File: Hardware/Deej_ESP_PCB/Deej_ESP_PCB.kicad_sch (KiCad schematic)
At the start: 110 parts, among them J1 USB_C_Receptacle_USB2.0_16P, P1 10K, P2 10K, P3 10K, P4 10K, P5 10K, P6 10K, SW1 SW_Push, SW2 SW_Push, SW3 SW_Push, SW4 SW_Push, SW5 SW_Push, SW6 SW_Push, U1 ESP32-S3-MINI-1U, U10 0.96" 128x64 OLED, U11 ECMF02-2AMX6, U2 PCF8574RGTR, U3 PCF8574RGTR, U4 PCF8574RGTR, U5 SN74HCS126DR, U6 SN74HCS126DR, U7 0.96" 128x64 OLED, U8 0.96" 128x64 OLED, U9 0.96" 128x64 OLED

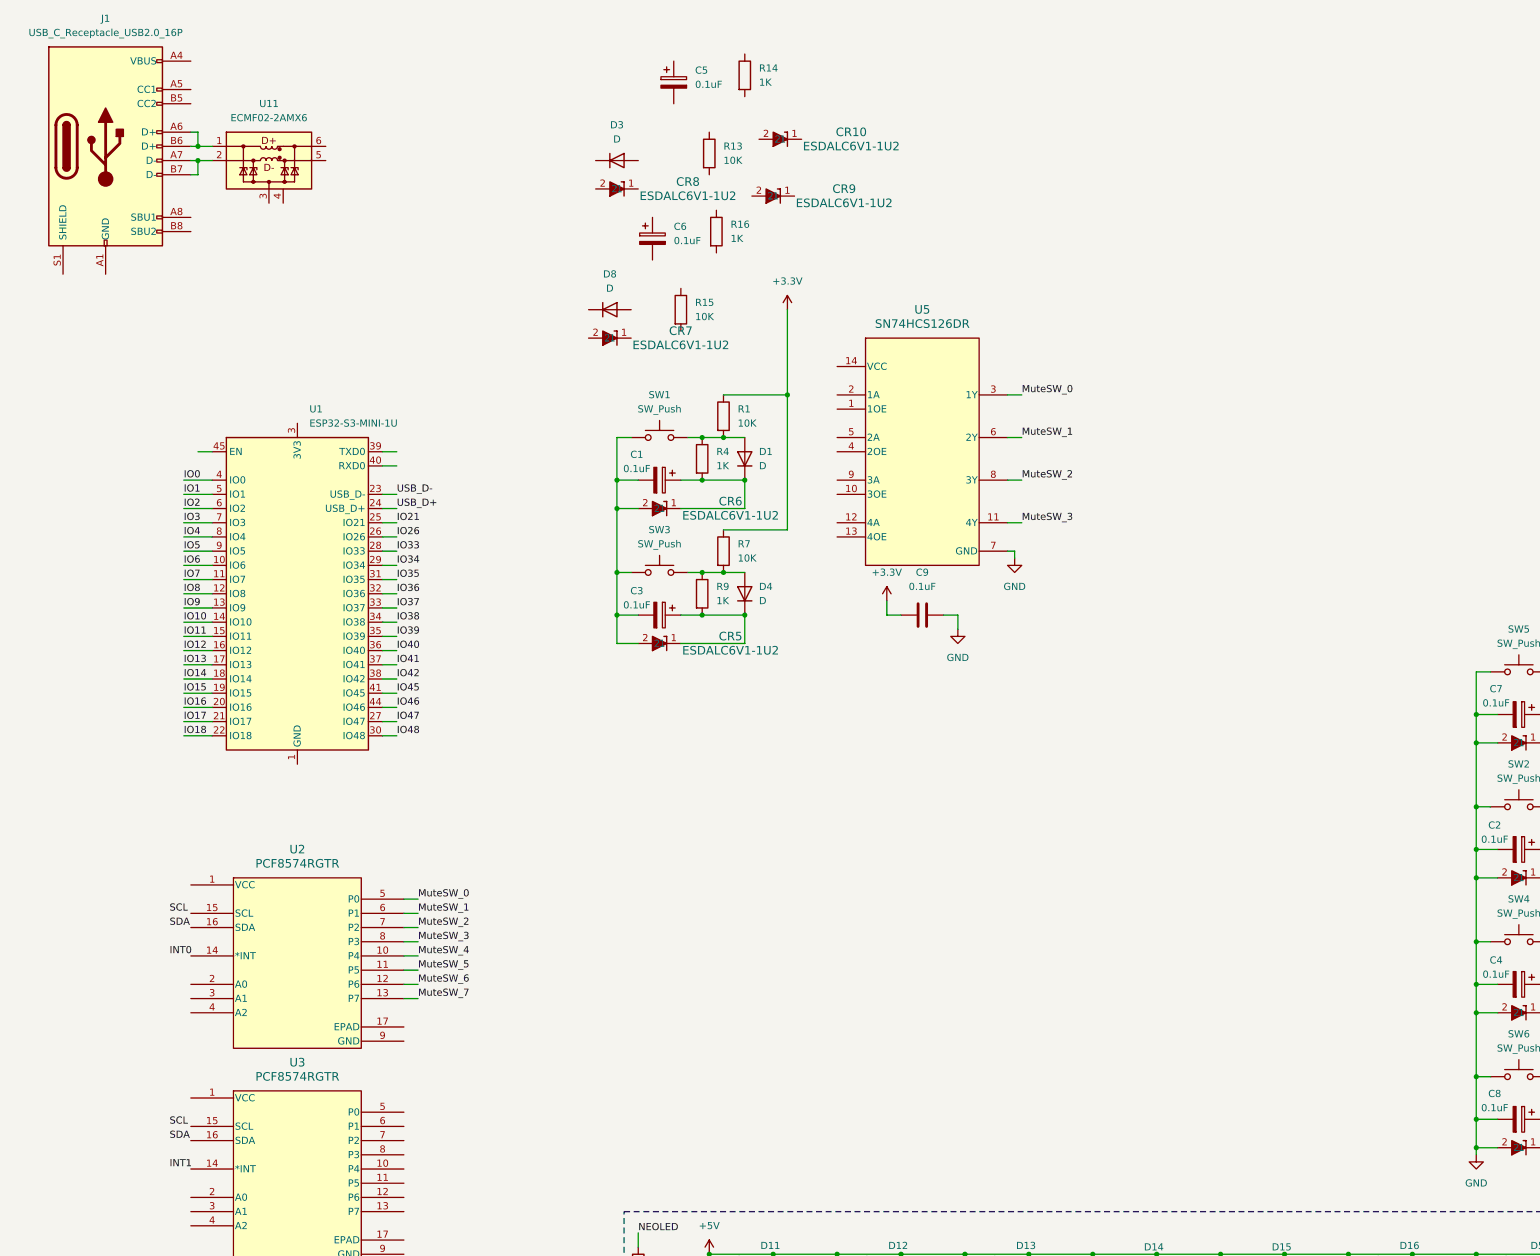
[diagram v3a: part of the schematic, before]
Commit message: USB Supporting Hardware, 3D Models, BOM Updates
* Added supporting hardware for the USB C connector
* Ensured all current components have 3D models
* Updated the BOM with components for the USB connector
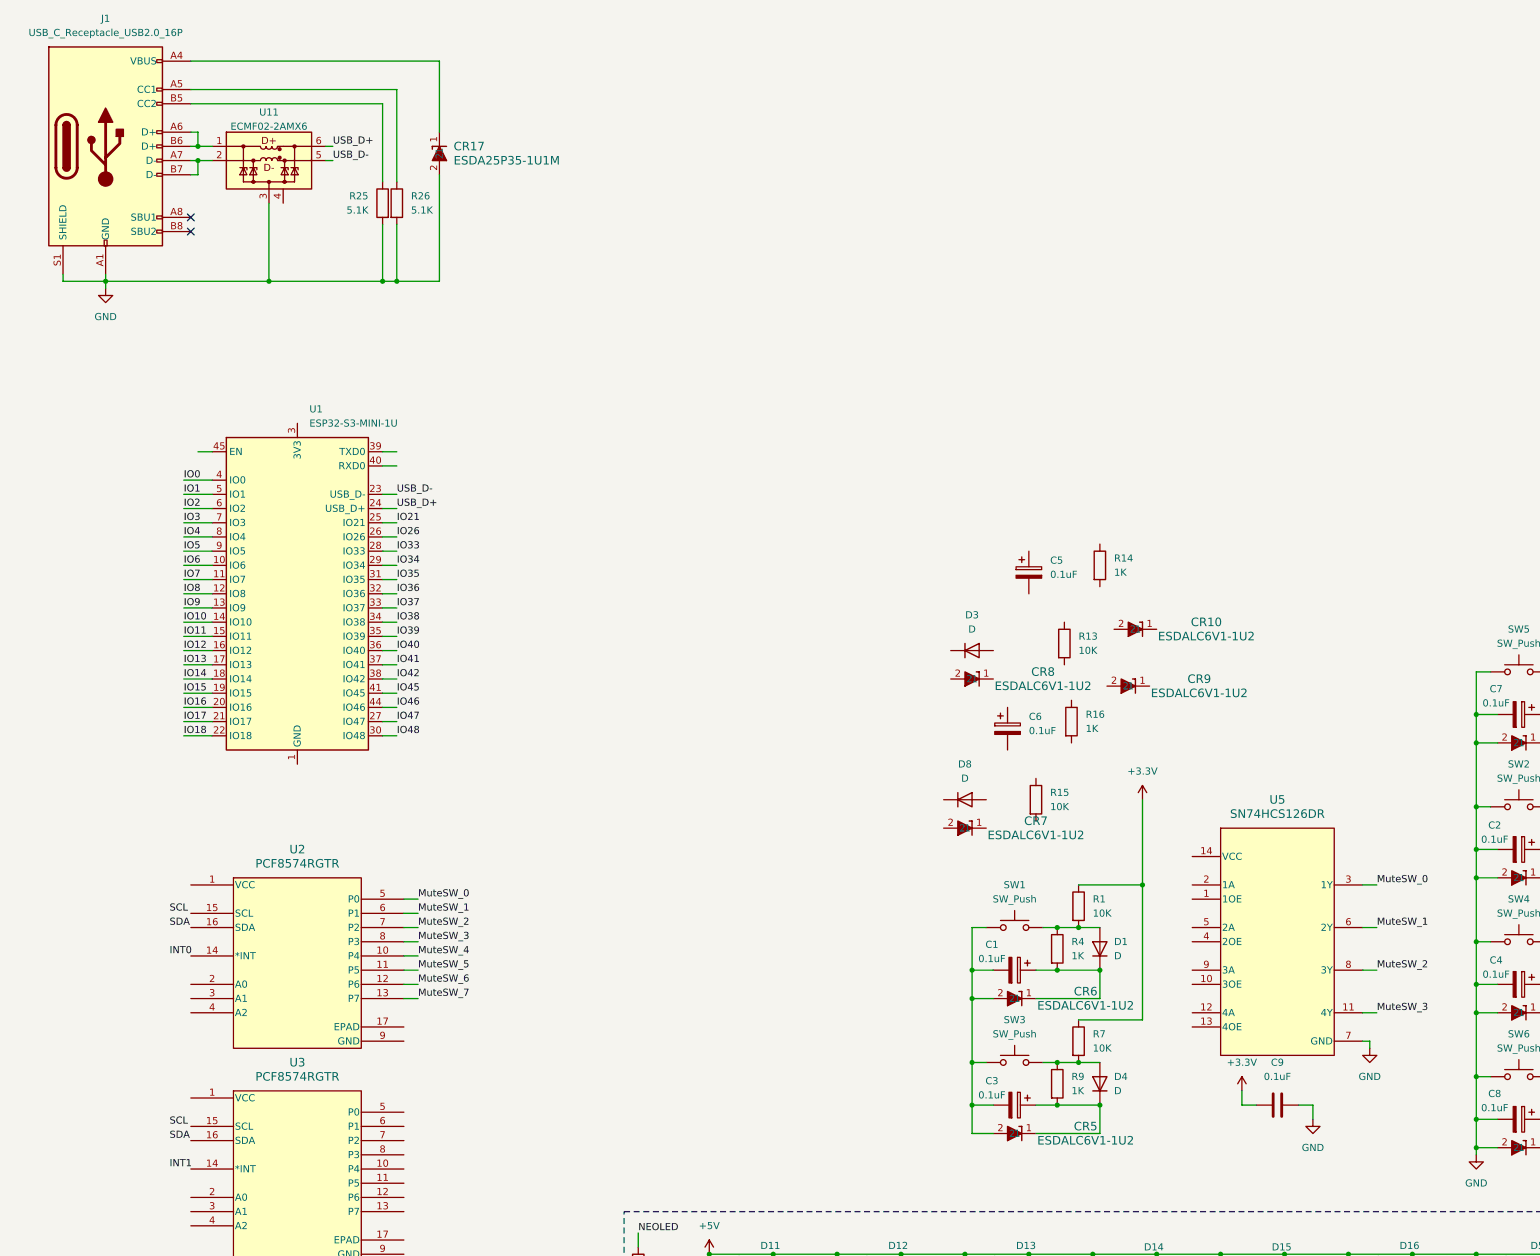
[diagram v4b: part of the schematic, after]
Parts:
- added CR17: ESDA25P35-1U1M, QFN1610_STM, symbol STM:ESDA25P35-1U1M
- added R25, R26: 5.1K, PCM_Resistor_SMD_AKL:R_0201_0603Metric_Pad0.64x0.40mm_HandSolder, symbol Device:R
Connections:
- net GND: now also J1.A1 (GND), J1.A12 (GND), J1.B1 (GND), J1.B12 (GND), J1.S1 (SHIELD), U11.3 (GND), CR17.2, R25.2, R26.2
- net USB_D+: now also U11.6 (D+_out)
- net USB_D-: now also U11.5 (D-_out)
- net at J1.A4 (VBUS), J1.A9 (VBUS), J1.B4 (VBUS)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: now also CR17.1
- net at J1.A5 (CC1): now also R26.1
- net at J1.B5 (CC2): now also R25.1
- no-connect marks 0 -> 2
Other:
- moved on the sheet: C1, C3, C5, C6, C9, CR10, CR5, CR6, CR7, CR8, CR9, D1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

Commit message: Added Footprints and 3D Files
- Added the proper footprint and 3D file for the ESP32
- Added the footprint and 3D file for the USB choke/ESD so the project
  doesn't rely on an external library
- Added the power step down circuit and LED indicators
- Added a user LED for program status
- Made a "Good Enough for Government Work" symbol and footprint for
  the Bourns rotary potentiometer I want to use while I wait for
  SamacSys
- Updated the BOM
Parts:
- removed U10, U7, U8, U9: 0.96" 128x64 OLED, symbol Adafruit:0_96_128x16_OLED_Module
- added C25, C26: 10uF, Capacitor_SMD:C_0603_1608Metric_Pad1.08x0.95mm_HandSolder, symbol Device:C
- added D23: Red LED, LED_SMD:LED_0603_1608Metric_Pad1.05x0.95mm_HandSolder, symbol Device:LED
- added D24: Orange LED, LED_SMD:LED_0603_1608Metric_Pad1.05x0.95mm_HandSolder, symbol Device:LED
- added D25: Green LED, LED_SMD:LED_0603_1608Metric_Pad1.05x0.95mm_HandSolder, symbol Device:LED
- added R27: 200, Capacitor_SMD:C_0603_1608Metric_Pad1.08x0.95mm_HandSolder, symbol Device:R
- added R28, R29: 100, Capacitor_SMD:C_0603_1608Metric_Pad1.08x0.95mm_HandSolder, symbol Device:R
- added U12: LMS1585ACS-3.3/NOPB, TI:KTT0003B, symbol TI:LMS1585ACS-3.3_NOPB
- added U13, U14: ~, Bourns_Potentiometer:39LA-1PB-103, symbol Bourns_Potentiometer:39LA-1PB-103
- added U15, U7, U8, U9: 1.3" 128x64 OLED, Adafruit_1_3_OLED, symbol Adafruit:1_3_128x64_OLED_Module
- C11, C12, C13, C14, C15, C16, C17, C18, C19, C20, C21, C22, C23, C24: footprint Capacitor_SMD:C_0201_0603Metric_Pad0.64x0.40mm_HandSolder -> Capacitor_SMD:C_0603_1608Metric_Pad1.08x0.95mm_HandSolder
- R1, R10, R11, R12, R13, R14, R15, R16, R17, R18, R19, R2, R20, R21, R22, R23, R24, R25, R26, R3, R4, R5, R6, R7, R8, R9: footprint PCM_Resistor_SMD_AKL:R_0201_0603Metric_Pad0.64x0.40mm_HandSolder -> Capacitor_SMD:C_0603_1608Metric_Pad1.08x0.95mm_HandSolder
- U1: footprint RF_Module:ESP32-S2-MINI-1U -> ESP32:ESP32S3MINI1UN8
- U11: footprint Package_DFN_QFN:ST_UQFN-6L_1.5x1.7mm_P0.5mm -> STM:QFN-6L_STM
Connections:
- net +3.3V: now also R13.1, R15.1, U5.1 (1OE), U5.10 (3OE), U5.13 (4OE), U5.14 (VCC), U5.4 (2OE), C26.1, R28.1, R29.1, U12.2 (OUTPUT), U12.4 (OUTPUT), U13.1, U14.1, U15.6 (3V3), U7.6 (3V3), U8.6 (3V3), U9.6 (3V3)
- net +5V: now also CR17.1, J1.A4 (VBUS), J1.A9 (VBUS), J1.B4 (VBUS), J1.B9 (VBUS), C25.1, R27.1, U12.3 (INPUT), U15.7 (VCC), U7.7 (VCC), U8.7 (VCC), U9.7 (VCC)
- net CS0: now also U15.5 (CS)
- net CS1: now also U7.5 (CS)
- net CS2: now also U8.5 (CS)
- net CS3: now also U9.5 (CS)
- net D/C: now also U15.3 (D/C), U7.3 (D/C), U8.3 (D/C), U9.3 (D/C)
- net GND: now also C1.2, C3.2, C5.2, C6.2, CR10.2, CR5.2, CR6.2, CR7.2, CR8.2, CR9.2, SW1.1, SW3.1, C25.2, C26.2, D23.1 (K), D24.1 (K), U12.1 (GND), U13.3, U13.A, U14.3, U14.A, U15.8 (GND), U7.8 (GND), U8.8 (GND), U9.8 (GND)
- net MOSI: now also U15.1 (MOSI), U7.1 (MOSI), U8.1 (MOSI), U9.1 (MOSI)
- net RST: now also U15.4 (RST), U7.4 (RST), U8.4 (RST), U9.4 (RST)
- net SCLK: now also U15.2 (SCLK), U7.2 (SCLK), U8.2 (SCLK), U9.2 (SCLK)
- net at D1.2 (A), R1.2, R4.1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: now also U5.9 (3A)
- net Analog_0: now reaches CR10.1
- net Analog_0: now also U14.2
- net at D8.1 (K): now also C6.1, CR7.1, R16.2
- net at D8.2 (A): now also R15.2, R16.1, U5.5 (2A), U13.B
- net at D4.2 (A), R7.2, R9.1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: now also U5.12 (4A)
- net at C5.1: now also CR8.1, D3.1 (K), R14.2
- net Analog_1: now reaches CR9.1
- net Analog_1: now also U13.2
- net at D3.2 (A): now also R13.2, R14.1, U5.2 (1A), U14.B
- new net: D25.2 (A), R29.2
- new net: D24.2 (A), R28.2
- new net: D23.2 (A), R27.2
- new net User LED: D25.1 (K)
- no-connect marks 2 -> 3
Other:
- title: (none) -> Deej Audi Controller ESP32-S3-MINI
- moved on the sheet: C1, C10, C2, C3, C4, C5, C6, C7, C8, C9, CR1, CR10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
